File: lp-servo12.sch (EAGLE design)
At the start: 63 parts, among them J1 M10", J2 M10", J3 M10", J4 M10", U1 TPS54526PWP, U2 LMV358

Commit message: Still learning git.  All my files were not in the last commit.
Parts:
- L1: device servoboard:MURATA-4900S -> kroesche:VISHAY-IHLP-3232DZ-11; MANF# (none) -> IHLP3232DZER3R3M11; MOUSER# (none) -> 70-IHLP3232DZER3R3M11
- R1: MANF (none) -> Panasonic; MANF# (none) -> ERJ-6GEYJ221V; MOUSER# (none) -> 667-ERJ-6GEYJ221V
- U1: device servoboard:TPS54526PWP -> kroesche:TPS54526PWP
- U2: MANF (none) -> Texas Instruments; MANF# (none) -> LMV358QDR; MOUSER# (none) -> 595-LMV358QDR
- X1: MANF (none) -> Molex; MANF# (none) -> 76650-0208; MOUSER# (none) -> 538-76650-0208
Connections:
- net GND: now also X1-1.S; no longer X1-2.S
- net VBAT: now also X1-2.S; no longer X1-1.S
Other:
- moved on the sheet: X1-1, X1-2
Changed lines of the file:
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@@
 <part name="SUPPLY3" library="supply2" deviceset="GND" device=""/>
 <part name="SUPPLY4" library="supply2" deviceset="GND" device=""/>
-<part name="X1" library="con-molex" deviceset="KK-156-2" device=""/>
+<part name="X1" library="con-molex" deviceset="KK-156-2" device="">
+<attribute name="MANF" value="Molex"/>
+<attribute name="MANF#" value="76650-0208"/>
+<attribute name="MOUSER#" value="538-76650-0208"/>
+</part>
 <part name="P+2" library="supply1" deviceset="+5V" device=""/>
-<part name="R1" library="SparkFun-Resistors" deviceset="RESISTOR" device="0805-RES" value="220"/>
+<part name="R1" library="SparkFun-Resistors" deviceset="RESISTOR" device="0805-RES" value="220">
+<attribute name="MANF" value="Panasonic"/>
+<attribute name="MANF#" value="ERJ-6GEYJ221V"/>
+<attribute name="MOUSER#" value="667-ERJ-6GEYJ221V"/>
+</part>
 <part name="STANDOFF1" library="SparkFun-Electromechanical" deviceset="STAND-OFF" device=""/>
 <part name="STANDOFF2" library="SparkFun-Electromechanical" deviceset="STAND-OFF" device=""/>
@@
 <part name="SUPPLY10" library="supply2" deviceset="GND" device=""/>
 <part name="SUPPLY11" library="supply2" deviceset="GND" device=""/>
-<part name="U1" library="servoboard" deviceset="TPS54526" device="PWP"/>
-<part name="L1" library="servoboard" deviceset="MURATA-4900S" device="" value="3.3uH"/>
+<part name="U1" library="kroesche" deviceset="TPS54526" device="PWP"/>
+<part name="L1" library="kroesche" deviceset="VISHAY-IHLP-3232DZ-11" device="" value="3.3uH">
+<attribute name="MANF#" value="IHLP3232DZER3R3M11"/>
+<attribute name="MOUSER#" value="70-IHLP3232DZER3R3M11"/>
+</part>
 <part name="FRAME1" library="SparkFun-Aesthetics" deviceset="FRAME-A3" device=""/>
 <part name="C7" library="SparkFun-Passives" deviceset="CAP" device="0805" value="100nF"/>
@@
 <part name="SUPPLY12" library="supply2" deviceset="GND" device=""/>
 <part name="SUPPLY5" library="supply2" deviceset="GND" device=""/>
-<part name="U2" library="SparkFun-AnalogIC" deviceset="LMV358" device=""/>
+<part name="U2" library="SparkFun-AnalogIC" deviceset="LMV358" device="">
+<attribute name="MANF" value="Texas Instruments"/>
+<attribute name="MANF#" value="LMV358QDR"/>
+<attribute name="MOUSER#" value="595-LMV358QDR"/>
+</part>
 <part name="R16" library="SparkFun-Resistors" deviceset="RESISTOR" device="0805-RES" value="22K"/>
 <part name="R17" library="SparkFun-Resistors" deviceset="RESISTOR" device="0805-RES" value="10K"/>
@@
 <instance part="SUPPLY3" gate="GND" x="33.02" y="132.08"/>
 <instance part="SUPPLY4" gate="GND" x="187.96" y="147.32"/>
-<instance part="X1" gate="-1" x="38.1" y="83.82" rot="MR0"/>
-<instance part="X1" gate="-2" x="38.1" y="78.74" rot="MR0"/>
+<instance part="X1" gate="-1" x="38.1" y="78.74" rot="MR0">
+<attribute name="MANF" x="38.1" y="78.74" size="1.778" layer="96" rot="MR0" display="off"/>
+<attribute name="MANF#" x="38.1" y="78.74" size="1.778" layer="96" rot="MR0" display="off"/>
+<attribute name="MOUSER#" x="38.1" y="78.74" size="1.778" layer="96" rot="MR0" display="off"/>
+</instance>
+<instance part="X1" gate="-2" x="38.1" y="83.82" rot="MR0"/>
 <instance part="P+2" gate="1" x="78.74" y="149.86"/>
-<instance part="R1" gate="G$1" x="43.18" y="233.68"/>
+<instance part="R1" gate="G$1" x="43.18" y="233.68">
+<attribute name="MANF" x="43.18" y="233.68" size="1.778" layer="96" display="off"/>
+<attribute name="MANF#" x="43.18" y="233.68" size="1.778" layer="96" display="off"/>
+<attribute name="MOUSER#" x="43.18" y="233.68" size="1.778" layer="96" display="off"/>
+</instance>
 <instance part="STANDOFF1" gate="G$1" x="363.22" y="27.94"/>
 <instance part="STANDOFF2" gate="G$1" x="368.3" y="27.94"/>
@@
 <instance part="SUPPLY12" gate="GND" x="185.42" y="40.64"/>
 <instance part="SUPPLY5" gate="GND" x="43.18" y="40.64"/>
-<instance part="U2" gate="G$1" x="231.14" y="165.1"/>
+<instance part="U2" gate="G$1" x="231.14" y="165.1">
+<attribute name="MANF" x="231.14" y="165.1" size="1.778" layer="96" display="off"/>
+<attribute name="MANF#" x="231.14" y="165.1" size="1.778" layer="96" display="off"/>
+<attribute name="MOUSER#" x="231.14" y="165.1" size="1.778" layer="96" display="off"/>
+</instance>
 <instance part="U2" gate="G$2" x="281.94" y="162.56"/>
 <instance part="R16" gate="G$1" x="274.32" y="177.8" smashed="yes">
@@
 <wire x1="185.42" y1="43.18" x2="185.42" y2="45.72" width="0.1524" layer="91"/>
 <junction x="185.42" y="45.72"/>
-<pinref part="X1" gate="-2" pin="S"/>
-<wire x1="40.64" y1="78.74" x2="43.18" y2="78.74" width="0.1524" layer="91"/>
 <wire x1="43.18" y1="78.74" x2="43.18" y2="45.72" width="0.1524" layer="91"/>
 <wire x1="43.18" y1="45.72" x2="50.8" y2="45.72" width="0.1524" layer="91"/>
@@
 <wire x1="43.18" y1="45.72" x2="43.18" y2="43.18" width="0.1524" layer="91"/>
 <junction x="43.18" y="45.72"/>
+<pinref part="X1" gate="-1" pin="S"/>
+<wire x1="40.64" y1="78.74" x2="43.18" y2="78.74" width="0.1524" layer="91"/>
 </segment>
 <segment>
@@
 <wire x1="83.82" y1="81.28" x2="83.82" y2="83.82" width="0.1524" layer="91"/>
 <junction x="83.82" y="83.82"/>
-<pinref part="X1" gate="-1" pin="S"/>
+<label x="44.704" y="85.344" size="1.778" layer="95"/>
+<pinref part="X1" gate="-2" pin="S"/>
 <wire x1="40.64" y1="83.82" x2="50.8" y2="83.82" width="0.1524" layer="91"/>
 <junction x="50.8" y="83.82"/>
-<label x="44.704" y="85.344" size="1.778" layer="95"/>
-</segment>
-<segment>
+</segment>
+<segment>

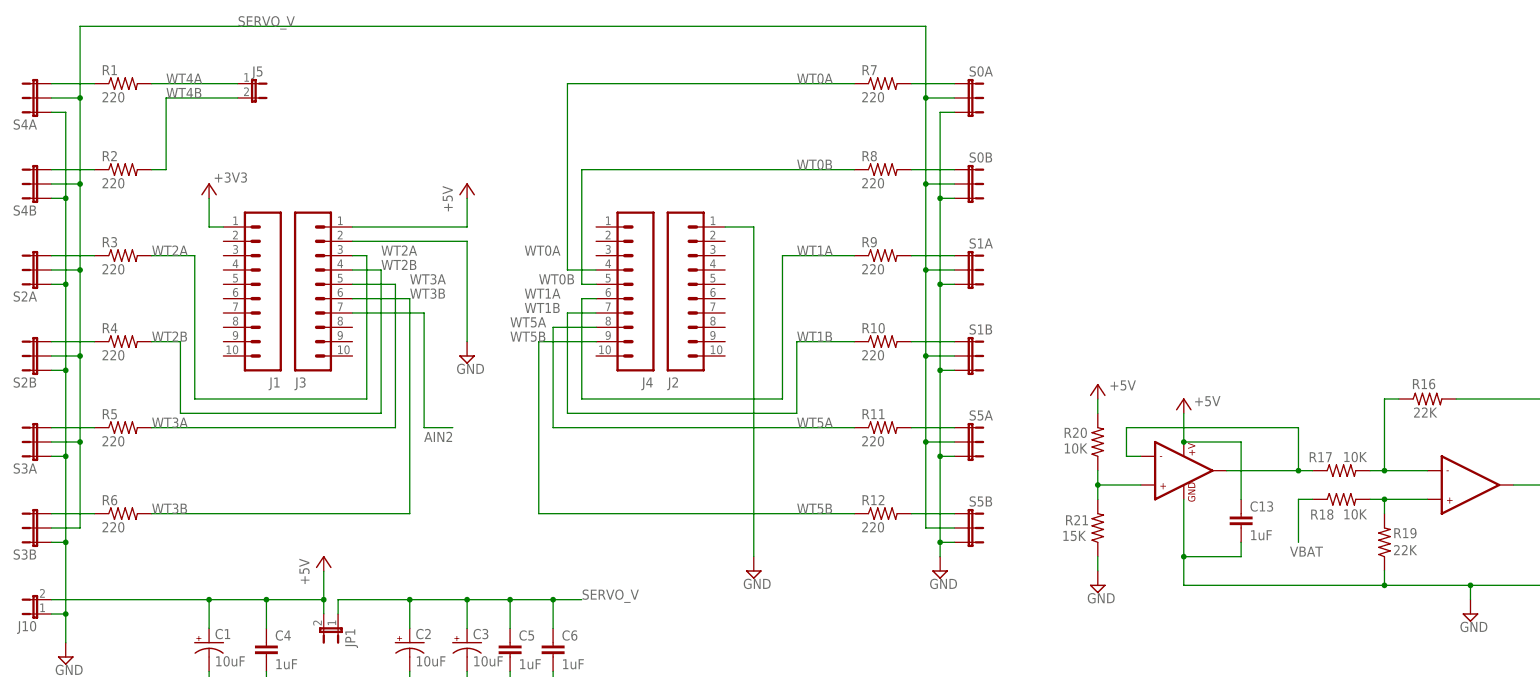
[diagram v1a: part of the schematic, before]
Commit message: Updated schematic part attributes so that bom-ex script can be used to generate a BOM.  Added parts database used and generated bom files (in bom/).
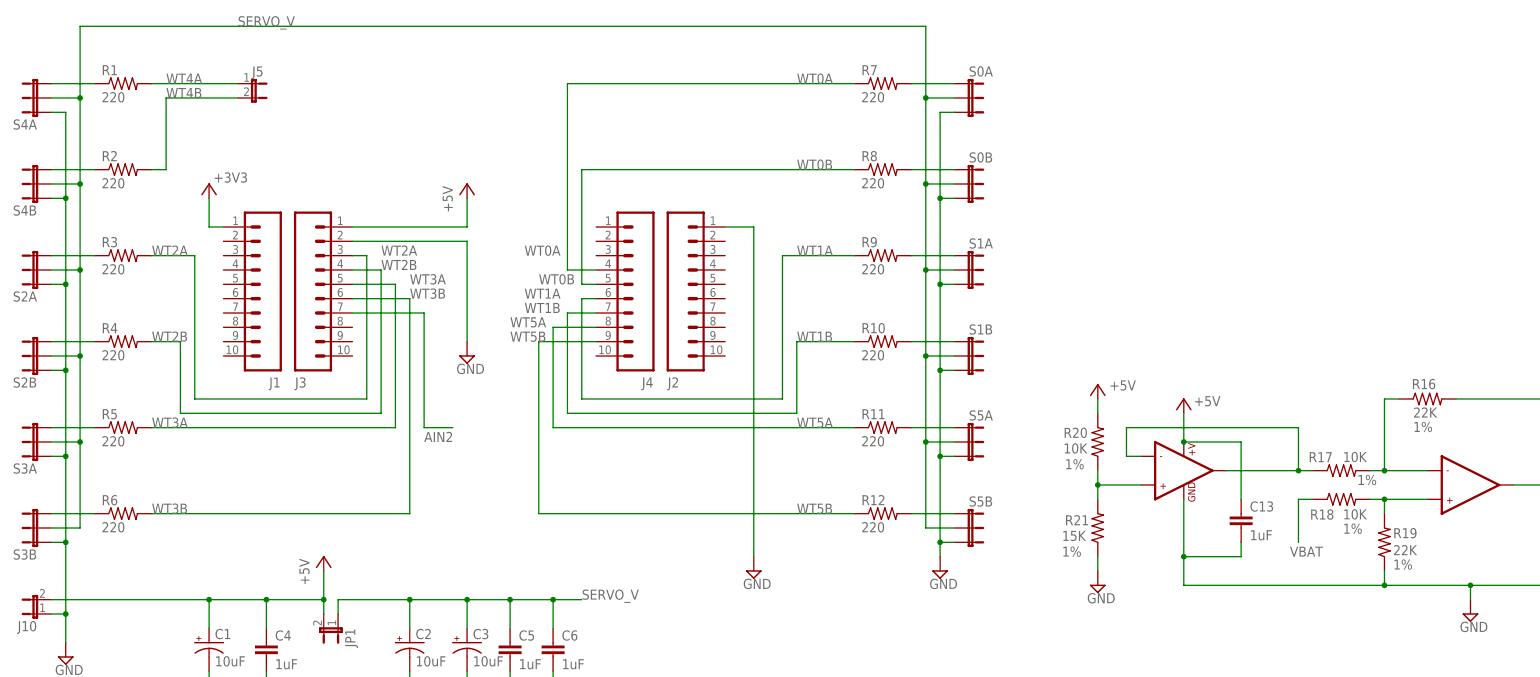
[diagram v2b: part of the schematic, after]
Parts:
- C1, C2, C3: PARTNO (none) -> CAP_10u_20V_20PCT_1206; SIZE (none) -> (1206); TOL (none) -> 20%; TYPE (none) -> TANT; VOLT (none) -> 20V
- C10: PARTNO (none) -> CAP_22u_16V_20PCT_1206; SIZE (none) -> (1206); TC (none) -> X5R; TOL (none) -> 20%; VOLT (none) -> 16V
- C11, C13, C14, C4, C5, C6: PARTNO (none) -> CAP_1u_20V_20PCT_0805; SIZE (none) -> (0805); TOL (none) -> 20%; VOLT (none) -> 20V
- C12: PARTNO (none) -> CAP_10n_50V_10PCT_0805; SIZE (none) -> (0805); TC (none) -> X7R; TOL (none) -> 10%; VOLT (none) -> 50V
- C7: PARTNO (none) -> CAP_100n_25V_10PCT_0805; SIZE (none) -> (0805); TC (none) -> X7R; TOL (none) -> 10%; VOLT (none) -> 25V
- C8: PARTNO (none) -> CAP_22p_50V_10PCT_0805; SIZE (none) -> (0805); TC (none) -> C0G; TOL (none) -> 10%; VOLT (none) -> 50V
- C9: PARTNO (none) -> CAP_22u_16V_10PCT_1210; SIZE (none) -> (1210); TC (none) -> X5R; TOL (none) -> 10%; VOLT (none) -> 16V
- J1, J2, J3, J4: PARTNO (none) -> 68002-110HLF
- J10: PARTNO (none) -> 68016-402
- J5, JP1: PARTNO (none) -> 68002-202HLF
- L1: LOAD (none) -> 10A; PARTNO (none) -> IHLP3232DZER3R3M11; TOL (none) -> 20%
- LOGO2, STANDOFF1, STANDOFF2, STANDOFF3, STANDOFF4: BOM (none) -> EXCLUDE
- R1, R10, R11, R12, R2, R3, R4, R5, R6, R7, R8, R9: PARTNO (none) -> RES_220_20V_10PCT_0805; SIZE (none) -> (0805); TOL (none) -> 10%; VOLT (none) -> 50V
- R13: PARTNO (none) -> RES_124K_20V_1PCT_0805; RATE (none) -> 1/8W; SIZE (none) -> (0805); TOL (none) -> 1%; VOLT (none) -> 20V
- R14: PARTNO (none) -> RES_22.1K_20V_1PCT_0805; RATE (none) -> 1/8W; SIZE (none) -> (0805); TOL (none) -> 1%; VOLT (none) -> 20V
- R15: PARTNO (none) -> RES_100K_20V_1PCT_0805; RATE (none) -> 1/8W; SIZE (none) -> (0805); TOL (none) -> 1%; VOLT (none) -> 20V
- R16, R19: PARTNO (none) -> RES_22K_20V_1PCT_0805; SIZE (none) -> (0805); TOL (none) -> 1%; VOLT (none) -> 20V
- R17, R18, R20: PARTNO (none) -> RES_10K_20V_1PCT_0805; SIZE (none) -> (0805); TOL (none) -> 1%; VOLT (none) -> 20V
- R21: PARTNO (none) -> RES_15K_20V_1PCT_0805; SIZE (none) -> (0805); TOL (none) -> 1%; VOLT (none) -> 20V
- S0A, S0B, S1A, S1B, S2A, S2B, S3A, S3B, S4A, S4B, S5A, S5B: PARTNO (none) -> 68002-403HLF
- U1: PARTNO (none) -> TPS54526PWP
- U2: PARTNO (none) -> LMV358QDR
- X1: PARTNO (none) -> KK-156-2-LOCK-RTANGLE

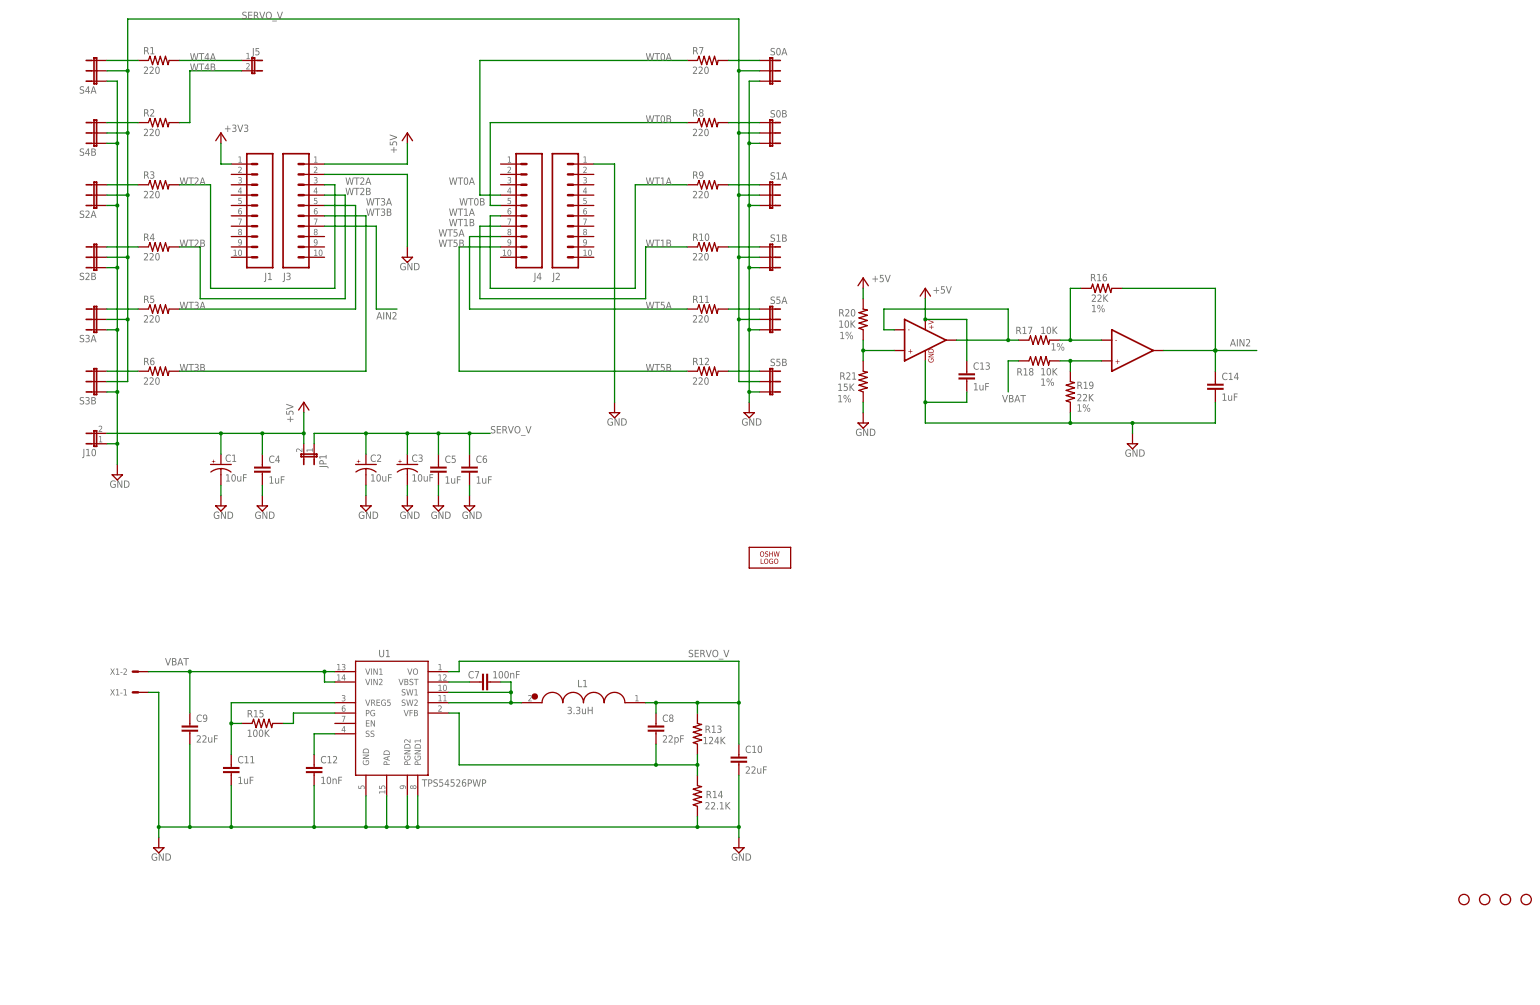
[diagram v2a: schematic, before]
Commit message: Added copyright and license text to board and schematic. Cosmetic changes only, no electrical or layout changes. Cleaned up schematic, added some comments. Change LICENSE to use creative commons attribution. Reflowed text in the README.
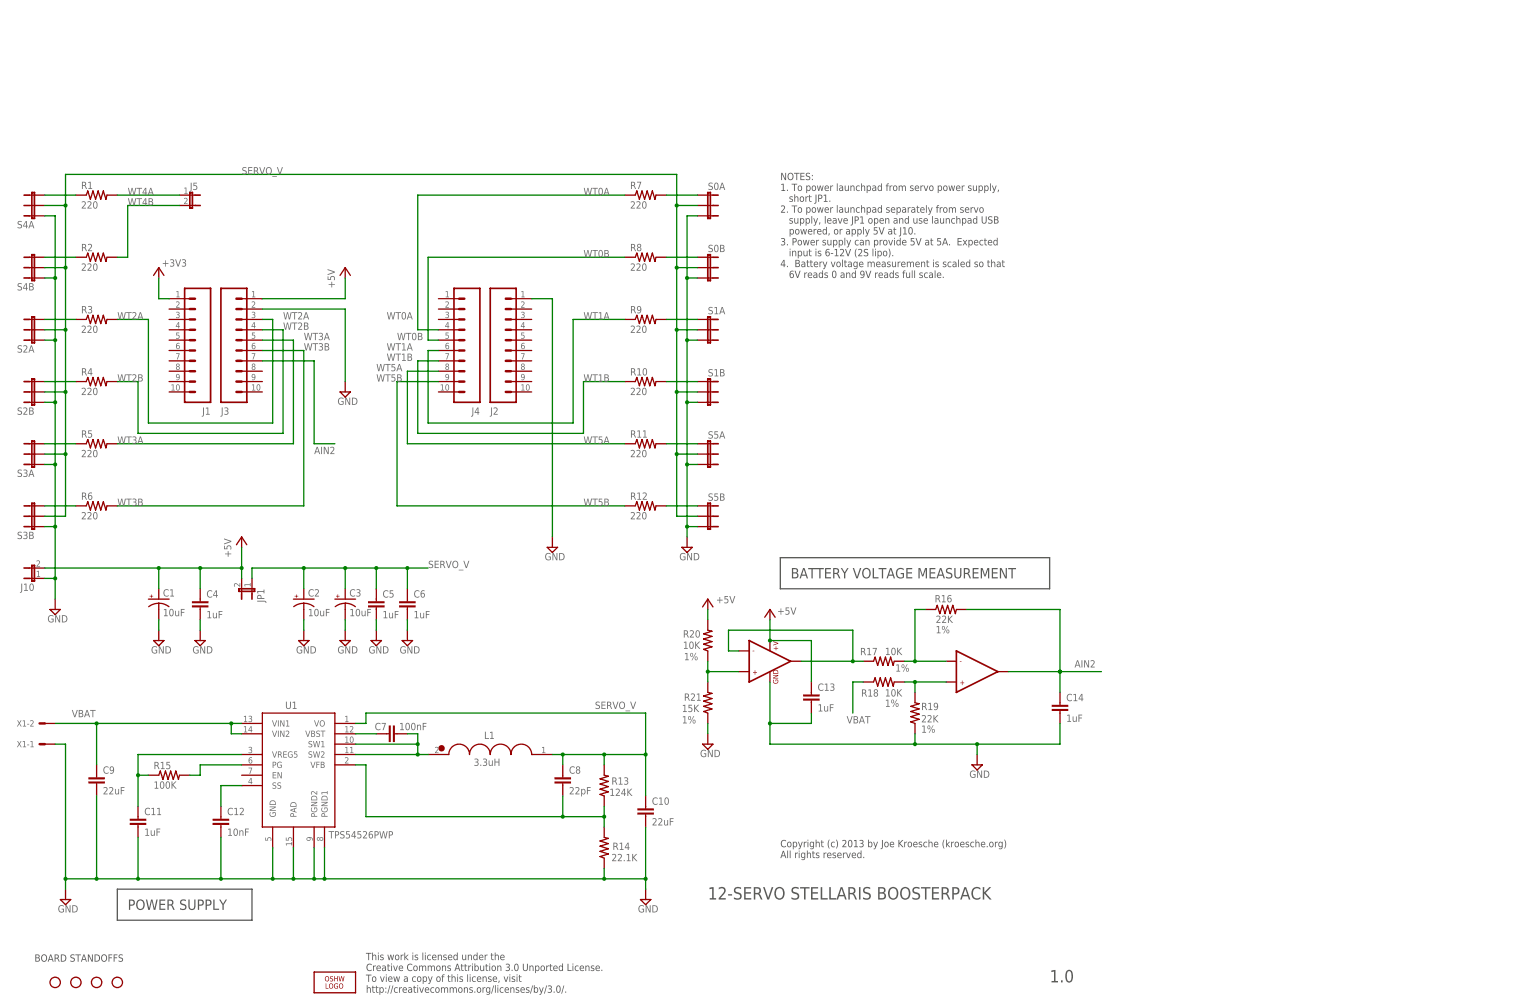
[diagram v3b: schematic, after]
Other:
- note added: "1.0"
- note added: "12-SERVO STELLARIS BOOSTERPACK"
- note added: "BATTERY VOLTAGE MEASUREMENT"
- note added: "BOARD STANDOFFS"
- note added: "Copyright (c) 2013 by Joe Kroesche (kroesche.org) All rights reserved."
- note added: "NOTES: 1. To power launchpad from servo power supply, short JP1. 2. To power launchpad separately from servo supply, leave JP1 open and use launchpad USB powered, or apply 5V at J10. 3. Power supply can provide 5V at 5A. Expected input is 6-12V (2S lipo). 4. Battery voltage measurement is scaled so that 6V reads 0 and 9V reads full scale."
- note added: "POWER SUPPLY"
- note added: "This work is licensed under the Creative Commons Attribution 3.0 Unported License. To view a copy of this license, visit http://creativecommons.org/licenses/by/3.0/."
- moved on the sheet: C1, C10, C11, C12, C13, C14, C2, C3, C4, C5, C6, C7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
